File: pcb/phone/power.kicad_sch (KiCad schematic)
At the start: 27 parts, among them CN1 S2B-PH-SM4-TB, U4 TPS63021DSJR, U5 TPS7A0218PDBVR, U6 MCP73831-2ACI/MC, U7 MAX17048G+T10

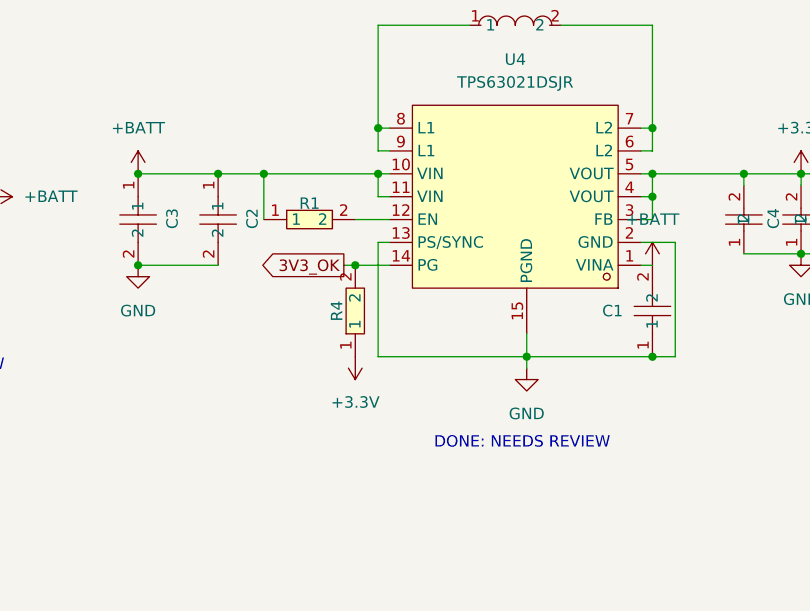
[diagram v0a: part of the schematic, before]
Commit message: Add power slide switch, modem bulk caps, reverse load switch decision
- SW1 (ALPS SSSS811101) added to power sheet: controls TPS63021 EN pin
  (ON: +BATT->R1->SW1->EN, OFF: EN->SW1->GND). Allows charging while off.
- C40 (470uF tantalum) + C41/C42 (10uF ceramic) added to modem sheet
  near MPCIe VCC pins for 2A+ LTE burst handling.
- Reversed load switch decision: SIM7600 sleep mode + PWRKEY make it
  redundant. Removed R11 (MCU_MODEM_PWR_EN pull-down), added no_connect
  on PE6.
- Registered temp_switch/temp_470uf/temp_10uf libraries in sym-lib-table
  and fp-lib-table (resolves 3 library-link ERC warnings).
- Final ERC: 0 errors, 6 warnings (all lib_symbol_mismatch, harmless).
- Updated docs: project-log, task-tracker, bom.

Generated with [Devin](https://devin.ai)

Co-Authored-By: Devin <158243242+devin-ai-integration[bot]@users.noreply.github.com>
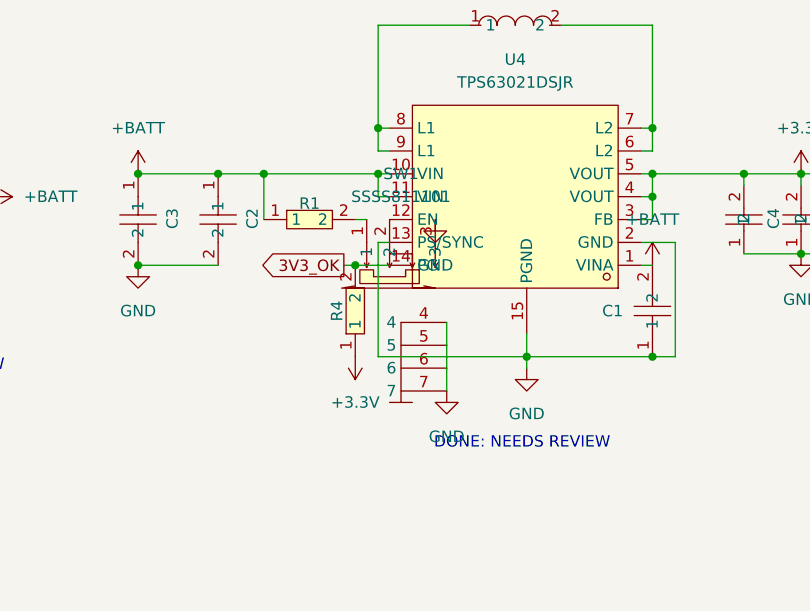
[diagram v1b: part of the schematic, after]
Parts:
- added SW1: SSSS811101, temp_switch:SW-SMD_SSSS811101, symbol temp_switch:SSSS811101
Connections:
- net GND: now also SW1.3, SW1.4, SW1.5, SW1.6, SW1.7
- net at R1.2: now also SW1.1; no longer U4.12 (EN)
- new net: SW1.2, U4.12 (EN)

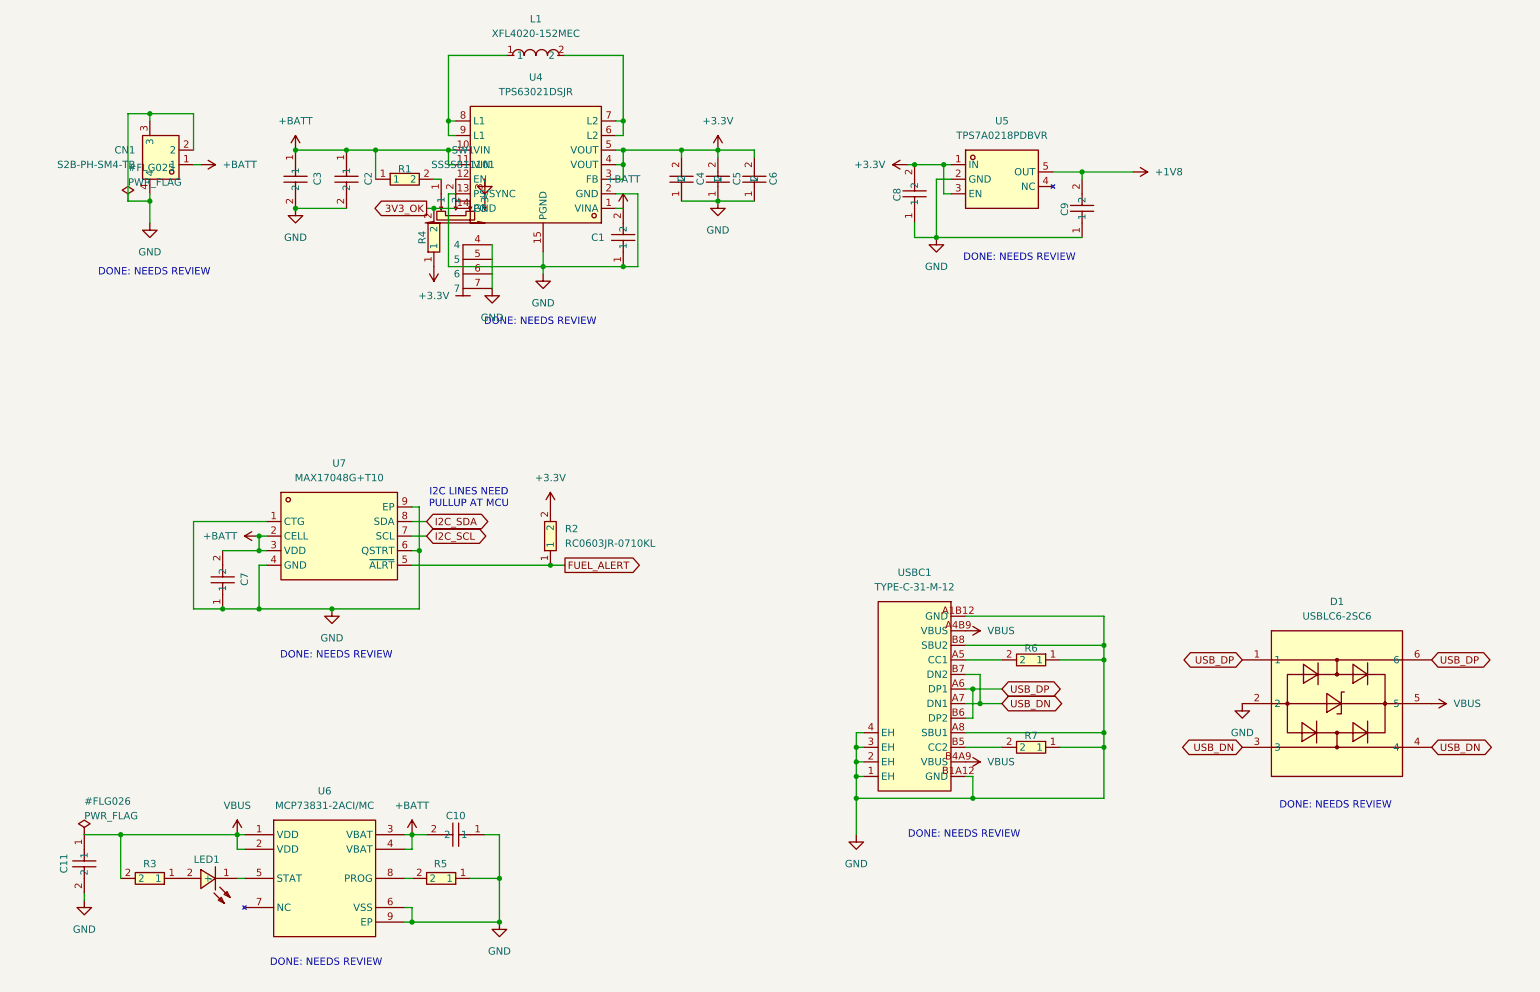
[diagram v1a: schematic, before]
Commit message: Cleanup: remove rejected part symbols, one-off scripts, stale datasheets
- Remove 7 rejected symbols from easyeda2kicad.kicad_sym (PJ-327C-4A,
  PJ-3250-5A, PJ-3240-5A, TYPE-C16PLC-H10.0, PJ-327A5JJ, PJ-327-P5,
  TYPEC-306DDW-ARP16) — replaced by Tensility 54-00298 and GCT USB4085-GF-A
- Delete 10 one-off inspection scripts (check_*.py, find_*.py, dump_*.py,
  extract_*.py) — keep only gen_*.py schematic generators
- Delete rejected datasheets (pj3126-5a, pj3240-5a, pj3250-5a, pj3f07-5p,
  N114 superseded display)
- Delete generated BOM/POS CSV files
- Add alps-ssss2.pdf and gct-usb4085.pdf to reference README index
- Include all schematic changes from previous sessions (SD pullups, VBUS
  divider fix, level shifter verification, codec caps, DCVDD fix)

Generated with [Devin](https://devin.ai)

Co-Authored-By: Devin <158243242+devin-ai-integration[bot]@users.noreply.github.com>
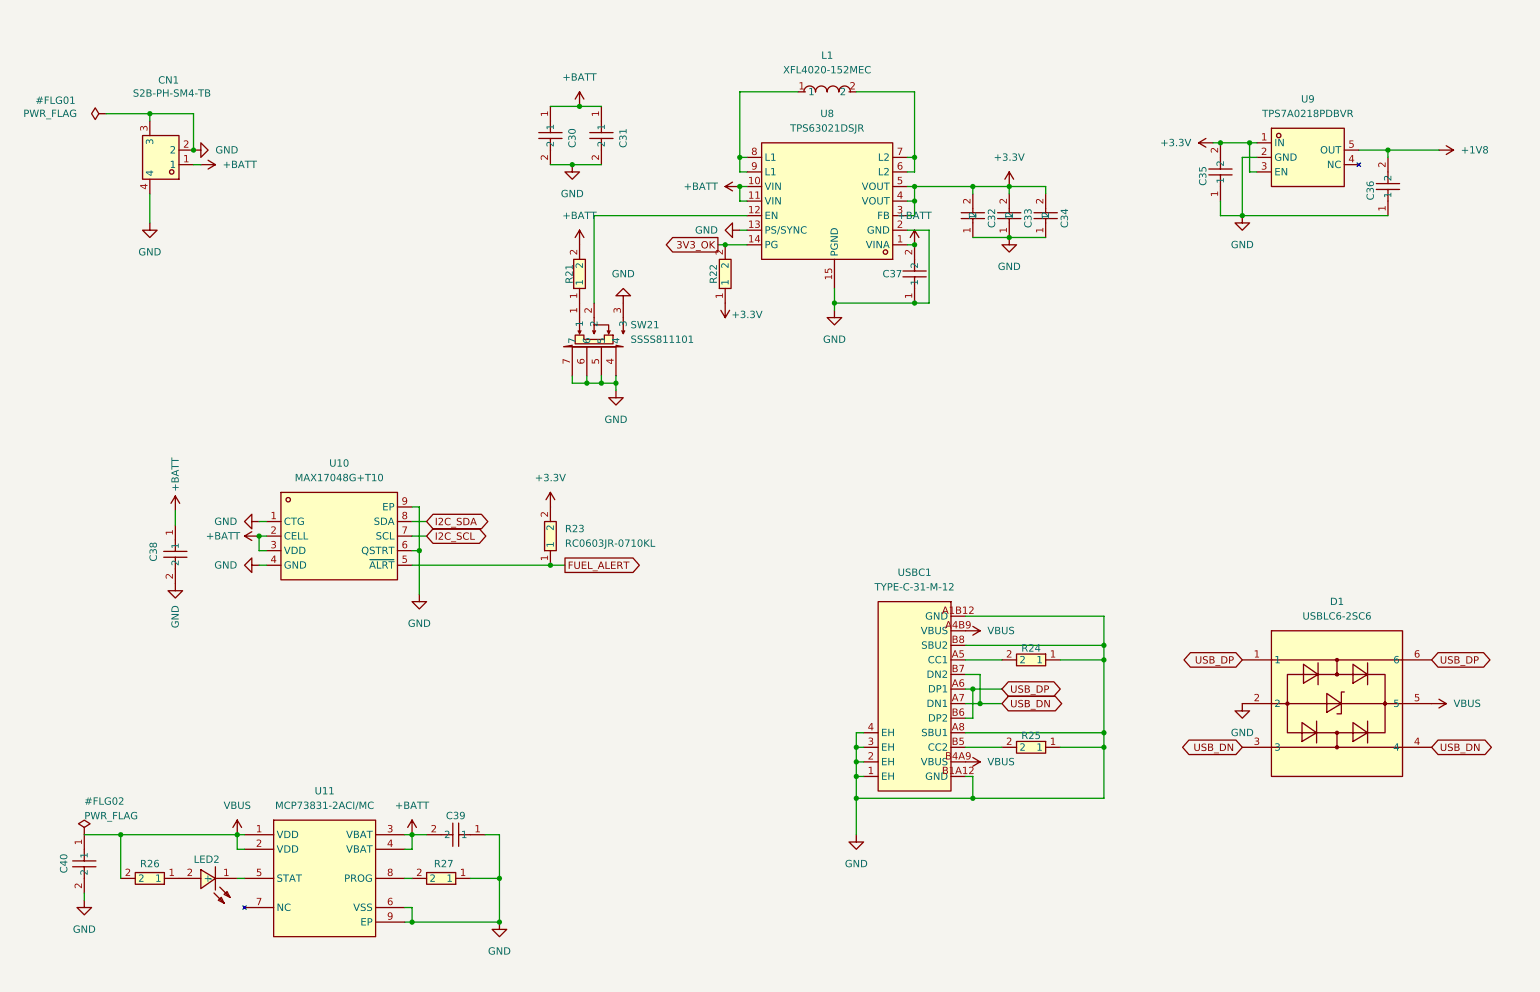
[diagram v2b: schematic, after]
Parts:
- renumbered C3 to C30, C2 to C31, C4 to C32, C5 to C33, C6 to C34, C8 to C35, C9 to C36, C1 to C37, C7 to C38, C10 to C39, C11 to C40, LED1 to LED2, R1 to R21, R4 to R22, R2 to R23, R6 to R24, R7 to R25, R3 to R26, R5 to R27, SW1 to SW21, U7 to U10, U6 to U11, U4 to U8, U5 to U9
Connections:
- net +BATT: now also C38.1, R21.2; no longer C38.2, R21.1
- net GND: now also C38.2; no longer C38.1
- net at SW21.1: now also R21.1; no longer R21.2
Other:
- note removed: "DONE: NEEDS REVIEW"
- note removed: "I2C LINES NEED PULLUP AT MCU"
- moved on the sheet: C30, C31, C32, C33, C34, C35, C36, C37, C38, L1, R21, R22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

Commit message: Project file audit cleanup: delete stale files, merge temp libs, fix docs
Delete stale/duplicate/garbage files identified by full project audit:
- easyeda2kicad.kicad_sym + missing_parts.kicad_sym (stale 1-symbol
  duplicates of symbols already in main libs; rebuild workflow broken)
- rebuild_lib.py + update_sch_refs.py + extract_pins.py (one-time
  migration scripts that no longer work — source files deleted)
- add_headphone_jack.py (dangerous — wiped codec sheet 2026-07-28)
- check_desc.py (one-off utility referencing stale file)
- main.kicad_sch (empty orphan, not referenced by project)
- bom_run.csv + 12 erc_*.txt + 2 ~*.lck (regenerable KiCad output)

Merge temp libraries into main libs (temp_switch/temp_470uf/temp_10uf):
- SSSS811101 slide switch -> electromech.kicad_sym
- 6TPF470MAH tantalum polymer -> passives.kicad_sym
- Footprints + 3D models moved to easyeda2kicad.pretty/3dshapes
- temp_10uf (CL10A106KP8NNNC) deleted — part was never placed
- Updated sym-lib-table, fp-lib-table, schematic lib_id/Footprint refs
- ERC validated: 0 errors, 15 warnings (all pre-existing types)

Fix documentation:
- lib/AGENTS.md: rewrote to reflect current state (4 libs are source
  of truth, no rebuild workflow, temp libs merged)
- .gitignore: removed 4 stale entries for gen_*.py at wrong paths
- research-notes.md: 3 [ ] -> [x] on RESOLVED items
- project-log.md: supersede note on 2026-07-22 entry + new audit entry
- datasheets/README.md: alps-ssss2.pdf -> alps-ssss8.pdf (wrong series
  datasheet — SSSS811101 is SSSS8 Series, not SSSS2; wrong LCSC # too)
- Downloaded correct alps-ssss8.pdf, deleted wrong alps-ssss2.pdf

Generated with [Devin](https://devin.ai)

Co-Authored-By: Devin <158243242+devin-ai-integration[bot]@users.noreply.github.com>
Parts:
- SW21: footprint temp_switch:SW-SMD_SSSS811101 -> easyeda2kicad:SW-SMD_SSSS811101; symbol temp_switch:SSSS811101 -> electromech:SSSS811101
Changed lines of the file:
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@@
 	)
 	(symbol
-		(lib_id "temp_switch:SSSS811101")
+		(lib_id "electromech:SSSS811101")
 		(at 115.57 71.12 0)
 		(unit 1)
@@
 			)
 		)
-		(property "Footprint" "temp_switch:SW-SMD_SSSS811101"
+		(property "Footprint" "easyeda2kicad:SW-SMD_SSSS811101"
 			(at 115.57 71.12 0)
 			(hide yes)

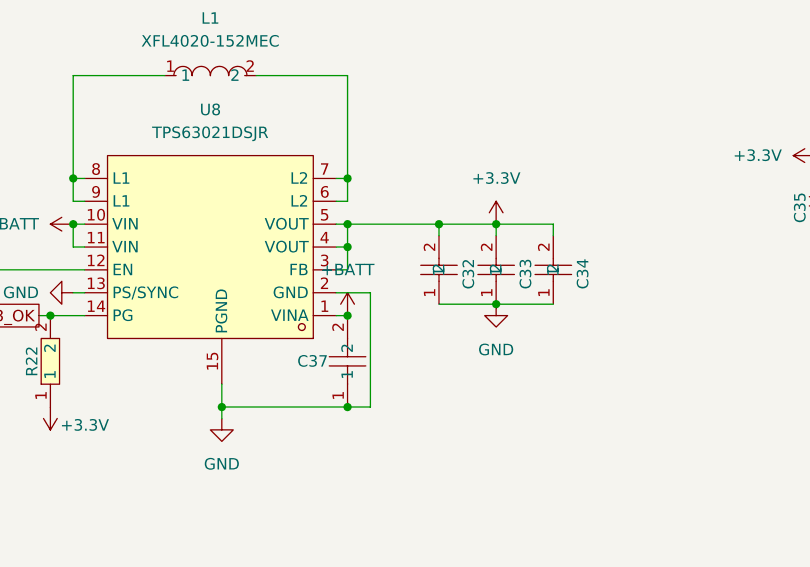
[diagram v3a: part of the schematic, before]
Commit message: Fix power sheet: isolate U8 VINA pin from +BATT, correct doc pin numbers
VINA (U8 pin 1) was wrongly tied to +BATT. Per TI TPS63021 datasheet Rev G,
VINA is internally supplied from VIN and must only connect to a 0.1uF bypass
cap (C37) to GND. External wiring reintroduces switching noise TI eliminated.
Added PWR_FLAG #FLG03 on the isolated VINA net to satisfy ERC.

Also fixed block-diagram.md line 66: pins 10/11 are VIN (not VOUT), pin 12
is EN. Corrected to "VIN (pin 10, 11) <- +BATT; VOUT (pin 4, 5) -> +3.3V"
and added missing 2x 10uF input caps to the component list.

ERC: 0 errors, 62 warnings (all pre-existing).

Generated with [Devin](https://devin.ai)

Co-Authored-By: Devin <158243242+devin-ai-integration[bot]@users.noreply.github.com>
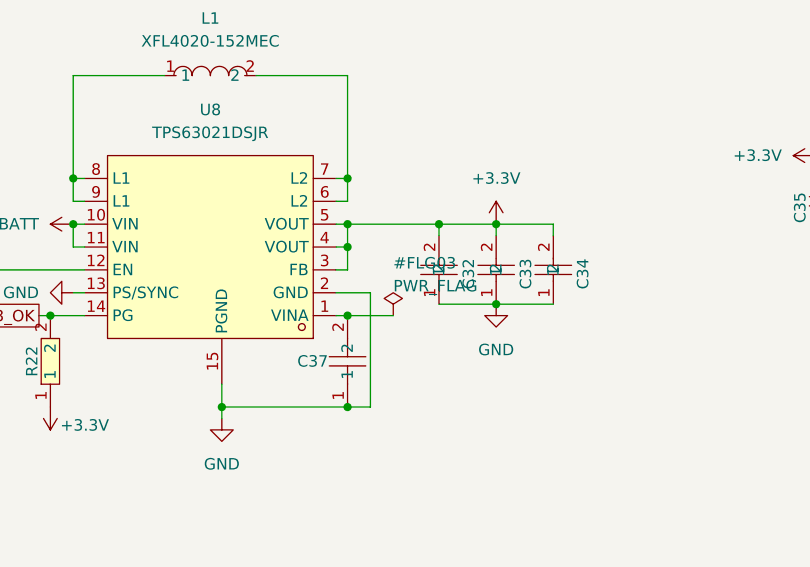
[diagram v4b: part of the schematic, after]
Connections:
- net +BATT: no longer C37.2, U8.1 (VINA)
- new net: C37.2, U8.1 (VINA)
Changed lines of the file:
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@@
 	(wire
 		(pts
+			(xy 168.91 50.8) (xy 170.18 50.8)
+		)
+		(stroke
+			(width 0)
+			(type default)
+		)
+	)
+	(wire
+		(pts
 			(xy 223.52 33.02) (xy 228.6 33.02)
 		)
@@
 	(wire
 		(pts
-			(xy 170.18 50.8) (xy 168.91 50.8)
-		)
-		(stroke
-			(width 0)
-			(type default)
-		)
-	)
-	(wire
-		(pts
 			(xy 41.275 99.695) (xy 41.275 97.155)
 		)
@@
 	(wire
 		(pts
+			(xy 170.18 50.8) (xy 175.26 50.8)
+		)
+		(stroke
+			(width 0)
+			(type default)
+		)
+	)
+	(wire
+		(pts
 			(xy 95.25 153.67) (xy 97.79 153.67)
 		)
@@
 	)
 	(symbol
-		(lib_id "power:+BATT")
-		(at 170.18 50.8 0)
-		(unit 1)
-		(body_style 1)
-		(exclude_from_sim no)
-		(in_bom yes)
-		(on_board yes)
-		(in_pos_files yes)
-		(dnp no)
-		(fields_autoplaced yes)
-		(property "Reference" "#PWR0169"
-			(at 170.18 54.61 0)
-			(hide yes)
-			(show_name no)
-			(do_not_autoplace no)
-			(effects
-				(font
-					(size 1.27 1.27)
-				)
-			)
-		)
-		(property "Value" "+BATT"
-			(at 170.18 45.72 0)
-			(show_name no)
-			(do_not_autoplace no)
-			(effects
-				(font
-					(size 1.27 1.27)
-				)
-			)
-		)
-		(property "Footprint" ""
-			(at 170.18 50.8 0)
-			(hide yes)
-			(show_name no)
-			(do_not_autoplace no)
-			(effects
-				(font
-					(size 1.27 1.27)
-				)
-			)
-		)
-		(property "Datasheet" ""
-			(at 170.18 50.8 0)
-			(hide yes)
-			(show_name no)
-			(do_not_autoplace no)
-			(effects
-				(font
-					(size 1.27 1.27)
-				)
-			)
-		)
-		(property "Description" ""
-			(at 170.18 50.8 0)
-			(show_name no)
-			(do_not_autoplace no)
-			(effects
-				(font
-					(size 1.27 1.27)
-				)
-			)
-		)
-		(pin "1"
-		)
-		(instances
-			(project "phone"
-				(path "/451c3b43-1616-42cb-bf96-d436f4db82c2/93995179-fee9-4317-80b0-38473b44bbe2"
-					(reference "#PWR0169")
-					(unit 1)
-				)
-			)
-		)
-	)
-	(symbol
 		(lib_id "passives:RC0603JR-0710KL")
 		(at 137.16 55.88 90)
@@
 					(unit 1)
 				)
+			)
+		)
+	)
+	(symbol
+		(lib_id "power:PWR_FLAG")
+		(at 175.26 50.8 0)
+		(unit 1)
+		(body_style 1)
+		(exclude_from_sim no)
+		(in_bom yes)
+		(on_board yes)
+		(in_pos_files yes)
+		(dnp no)
+		(fields_autoplaced yes)
+		(property "Reference" "#FLG03"
+			(at 175.26 45.72 0)
+			(show_name no)
+			(do_not_autoplace no)
+			(effects
+				(font
+					(size 1.27 1.27)
+				)
+				(justify left bottom)
+			)
+		)
+		(property "Value" "PWR_FLAG"
+			(at 175.26 48.26 0)
+			(show_name no)
+			(do_not_autoplace no)
+			(effects
+				(font
+					(size 1.27 1.27)
+				)
+				(justify left bottom)
+			)
+		)
+		(property "Footprint" ""
+			(at 175.26 50.8 0)
+			(hide yes)
+			(show_name no)
+			(do_not_autoplace no)
+			(effects
+				(font
+					(size 1.27 1.27)
+				)
+			)
+		)
+		(property "Datasheet" ""
+			(at 175.26 50.8 0)
+			(hide yes)
+			(show_name no)
+			(do_not_autoplace no)
+			(effects
+				(font
+					(size 1.27 1.27)
+				)
+			)
+		)
+		(property "Description" ""
+			(at 175.26 50.8 0)
+			(show_name no)
+			(do_not_autoplace no)
+			(effects
+				(font
+					(size 1.27 1.27)
+				)
+			)
+		)
+		(pin "1"
+		)
+		(instances
+			(project "phone"
+				(path "/451c3b43-1616-42cb-bf96-d436f4db82c2/93995179-fee9-4317-80b0-38473b44bbe2"
+					(reference "#FLG03")
+					(unit 1)
+				)
